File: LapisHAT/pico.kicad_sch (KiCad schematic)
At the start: 3 parts, among them J1 Conn_01x02, J2 Conn_02x20_Odd_Even

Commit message: Initial schematic
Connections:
- net ESC0: now also A1.14 (GPIO10); no longer A1.6 (GPIO4)
- net ESC1: now also A1.15 (GPIO11); no longer A1.7 (GPIO5)
- net ESC2: now also A1.16 (GPIO12); no longer A1.9 (GPIO6)
- net ESC3: now also A1.17 (GPIO13); no longer A1.10 (GPIO7)
- net ESC4: now also A1.19 (GPIO14); no longer A1.11 (GPIO8)
- net ESC5: now also A1.20 (GPIO15); no longer A1.12 (GPIO9)
- net LED0: now also A1.11 (GPIO8); no longer A1.19 (GPIO14)
- net LED1: now also A1.12 (GPIO9); no longer A1.20 (GPIO15)
- net MOTOR0_DIR: now also A1.1 (GPIO0); no longer A1.2 (GPIO1)
- net MOTOR0_PWM: now also A1.6 (GPIO4); no longer A1.1 (GPIO0)
- net MOTOR1_DIR: now also A1.2 (GPIO1); no longer A1.25 (GPIO19)
- net MOTOR1_PWM: now also A1.7 (GPIO5); no longer A1.24 (GPIO18)
- net MOTOR2_DIR: now also A1.4 (GPIO2); no longer A1.21 (GPIO16)
- net MOTOR2_PWM: now also A1.9 (GPIO6); no longer A1.22 (GPIO17)
- net MOTOR3_DIR: now also A1.5 (GPIO3); no longer A1.4 (GPIO2)
- net MOTOR3_PWM: now also A1.10 (GPIO7); no longer A1.5 (GPIO3)
- net SERVO0: now also A1.21 (GPIO16); no longer A1.14 (GPIO10)
- net SERVO1: now also A1.22 (GPIO17); no longer A1.15 (GPIO11)
- net SERVO2: now also A1.24 (GPIO18); no longer A1.16 (GPIO12)
- net SERVO3: now also A1.25 (GPIO19); no longer A1.17 (GPIO13)
- no-connect marks 39 -> 41

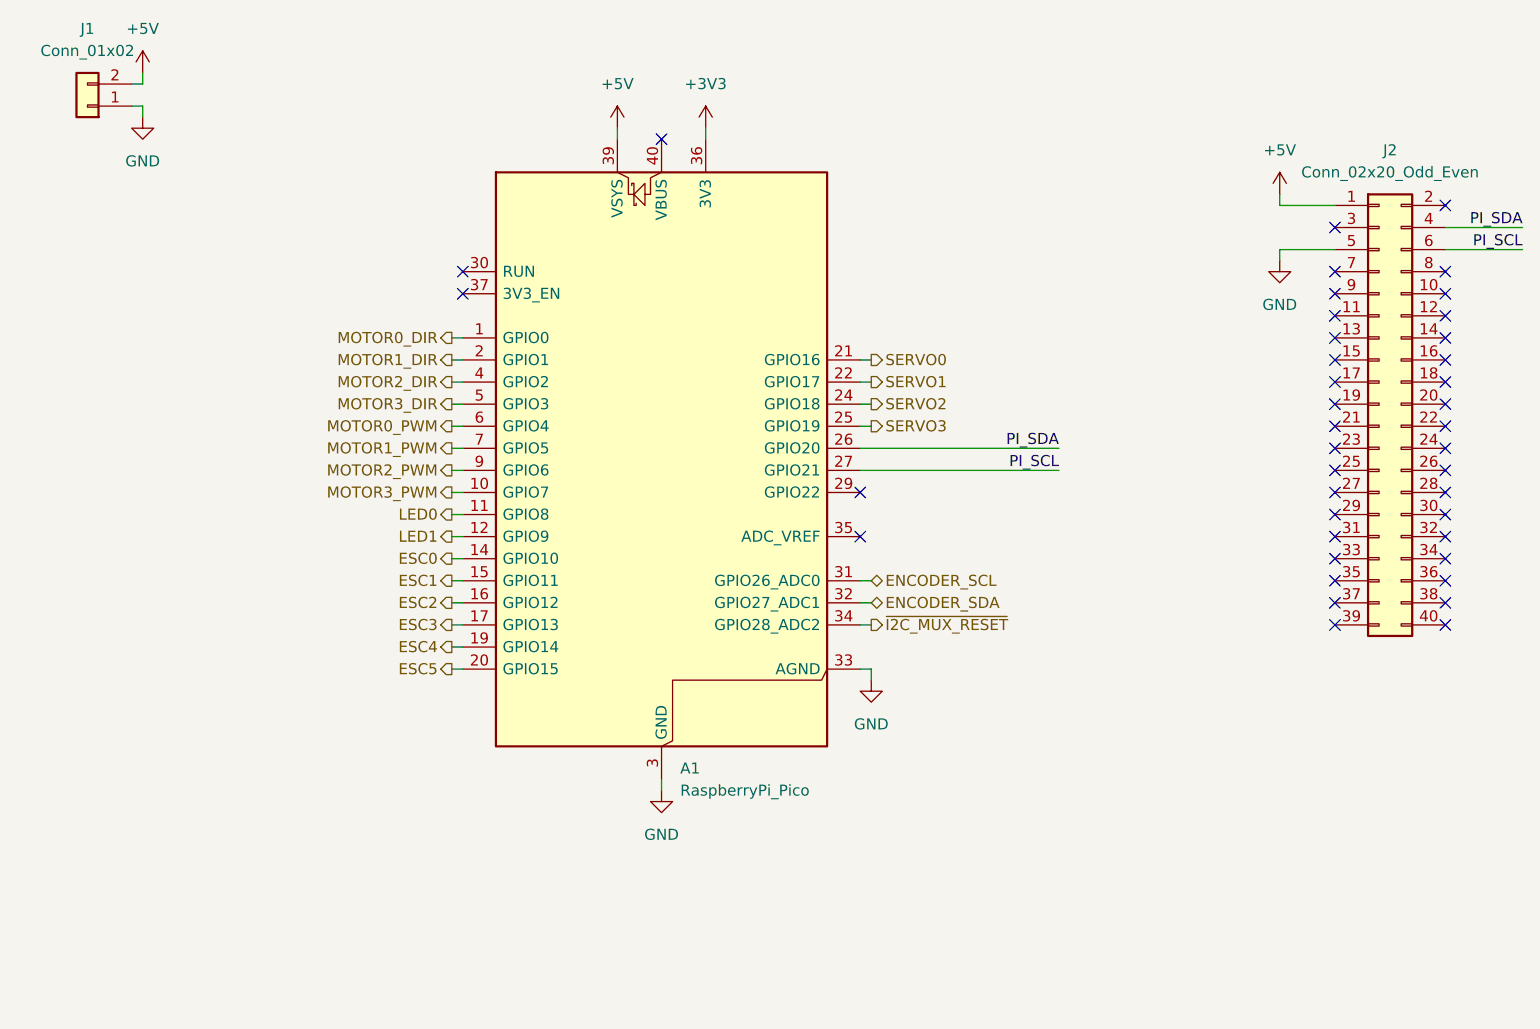
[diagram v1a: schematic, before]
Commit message: New Lapis Hat
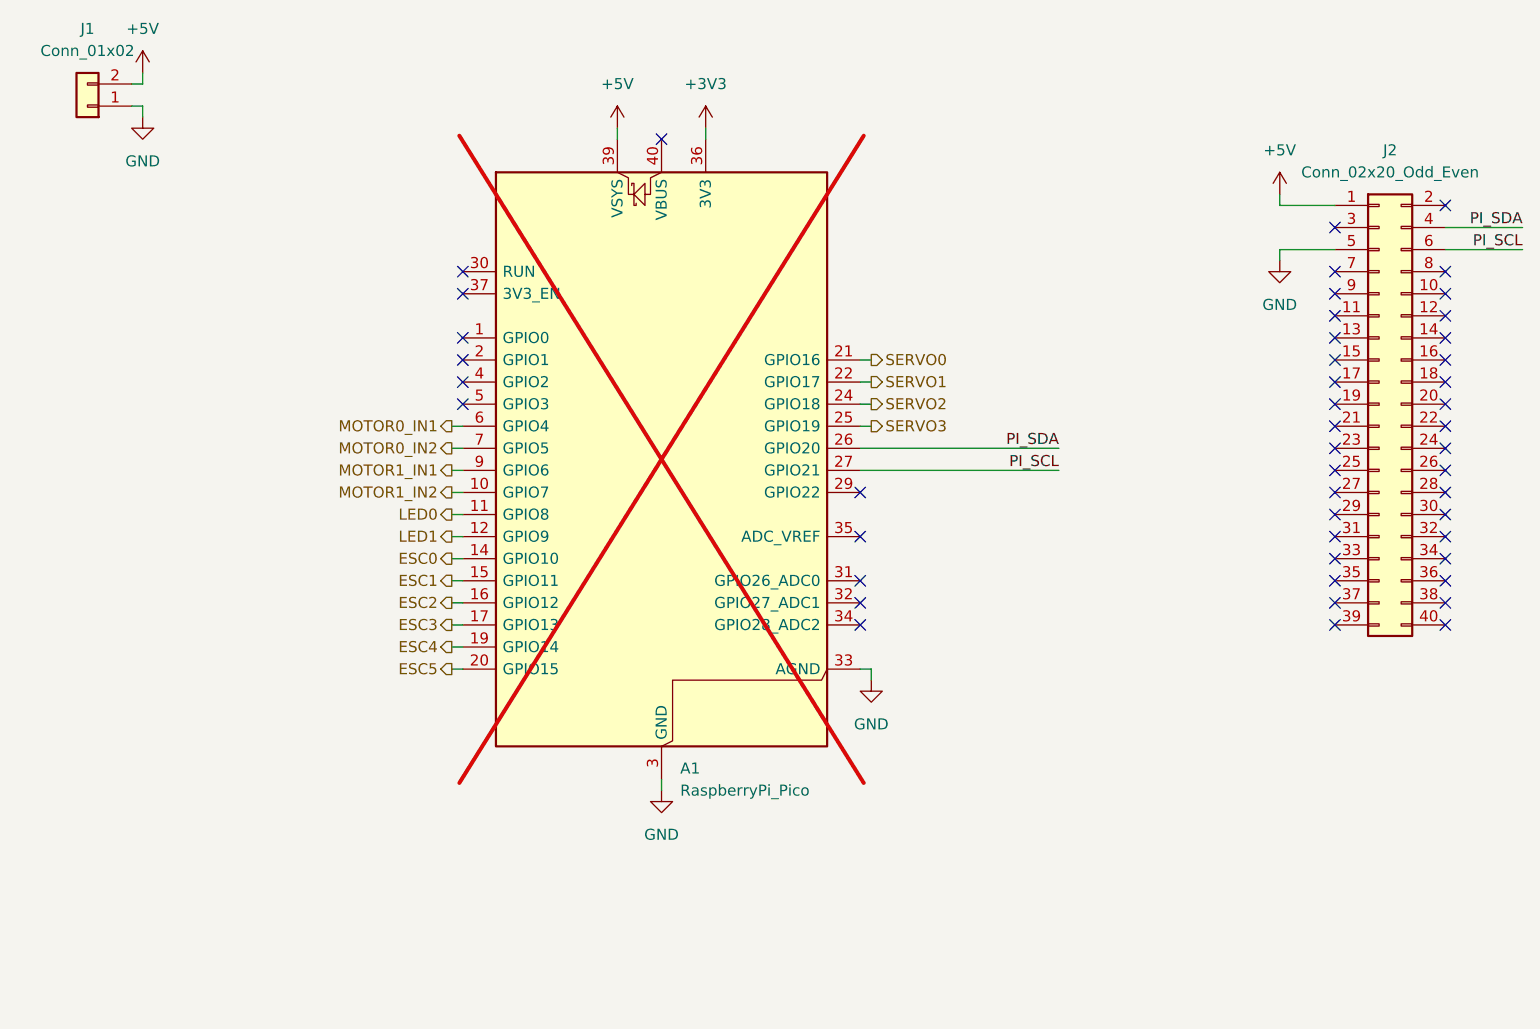
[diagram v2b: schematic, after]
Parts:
- A1: now not fitted
- J1: footprint Connector_PinHeader_2.54mm:PinHeader_1x02_P2.54mm_Vertical -> footprints:Molex-43650-0227_-MFG; LCSC (none) -> C585468
- J2: LCSC (none) -> C132132
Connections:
- net ENCODER_SCL: no longer names the net of A1.31 (GPIO26_ADC0)
- net ENCODER_SDA: no longer names the net of A1.32 (GPIO27_ADC1)
- net MOTOR0_DIR: no longer names the net of A1.1 (GPIO0)
- net MOTOR0_PWM renamed MOTOR0_IN1
- net MOTOR1_DIR: no longer names the net of A1.2 (GPIO1)
- net MOTOR1_PWM renamed MOTOR0_IN2
- net MOTOR2_DIR: no longer names the net of A1.4 (GPIO2)
- net MOTOR2_PWM renamed MOTOR1_IN1
- net MOTOR3_DIR: no longer names the net of A1.5 (GPIO3)
- net MOTOR3_PWM renamed MOTOR1_IN2
- net ~{I2C_MUX_RESET}: no longer names the net of A1.34 (GPIO28_ADC2)
- no-connect marks 41 -> 48

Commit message: Some review changes
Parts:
- added C3: 100u, Capacitor_SMD:CP_Elec_6.3x7.7, symbol Device:C_Polarized_Small_US
- added D1, D2, D3: LED, LED_SMD:LED_0603_1608Metric, symbol Device:LED
- added R10, R11: 4.7k, Resistor_SMD:R_0603_1608Metric, symbol Device:R_Small_US
- added R7: 100, Resistor_SMD:R_0603_1608Metric, symbol Device:R_Small_US
- added R8: 330, Resistor_SMD:R_0603_1608Metric, symbol Device:R_Small_US
- added R9: 2k, Resistor_SMD:R_0603_1608Metric, symbol Device:R_Small_US
- added TP1, TP2, TP4, TP5, TP6: TestPoint, TestPoint:TestPoint_Pad_2.0x2.0mm, symbol Connector:TestPoint
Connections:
- net +3V3: now also R10.1, R11.1, R7.1
- net +5V: now also C3.1, R8.1, TP2.1
- net GND: now also D1.1 (K), D2.1 (K), D3.1 (K), TP4.1
- net PI_SCL: now also R11.2, TP6.1
- net PI_SDA: now also R10.2, TP5.1
- new net: D1.2 (A), R7.2
- new net: D2.2 (A), R8.2
- new net: D3.2 (A), R9.2
- new net +12V: R9.1, TP1.1
